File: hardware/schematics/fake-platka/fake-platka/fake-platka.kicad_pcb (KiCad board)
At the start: 2 copper layers, 13.5 x 1.1 mm, 27 parts, among them J1 XT60PW-F, J2 XT60PW-F, J3 B2B-EH-A, J4 B2B-EH-A, J5 B2B-EH-A, J6 B2B-EH-A, J7 B2B-EH-A, J8 XT60PW-F, J9 XT60PW-F, U1 XL4005, U2 TB67H450AFNG_EL, U3 TB67H450AFNG_EL, U4 SC0915-pico-w-board, U5 XL4005

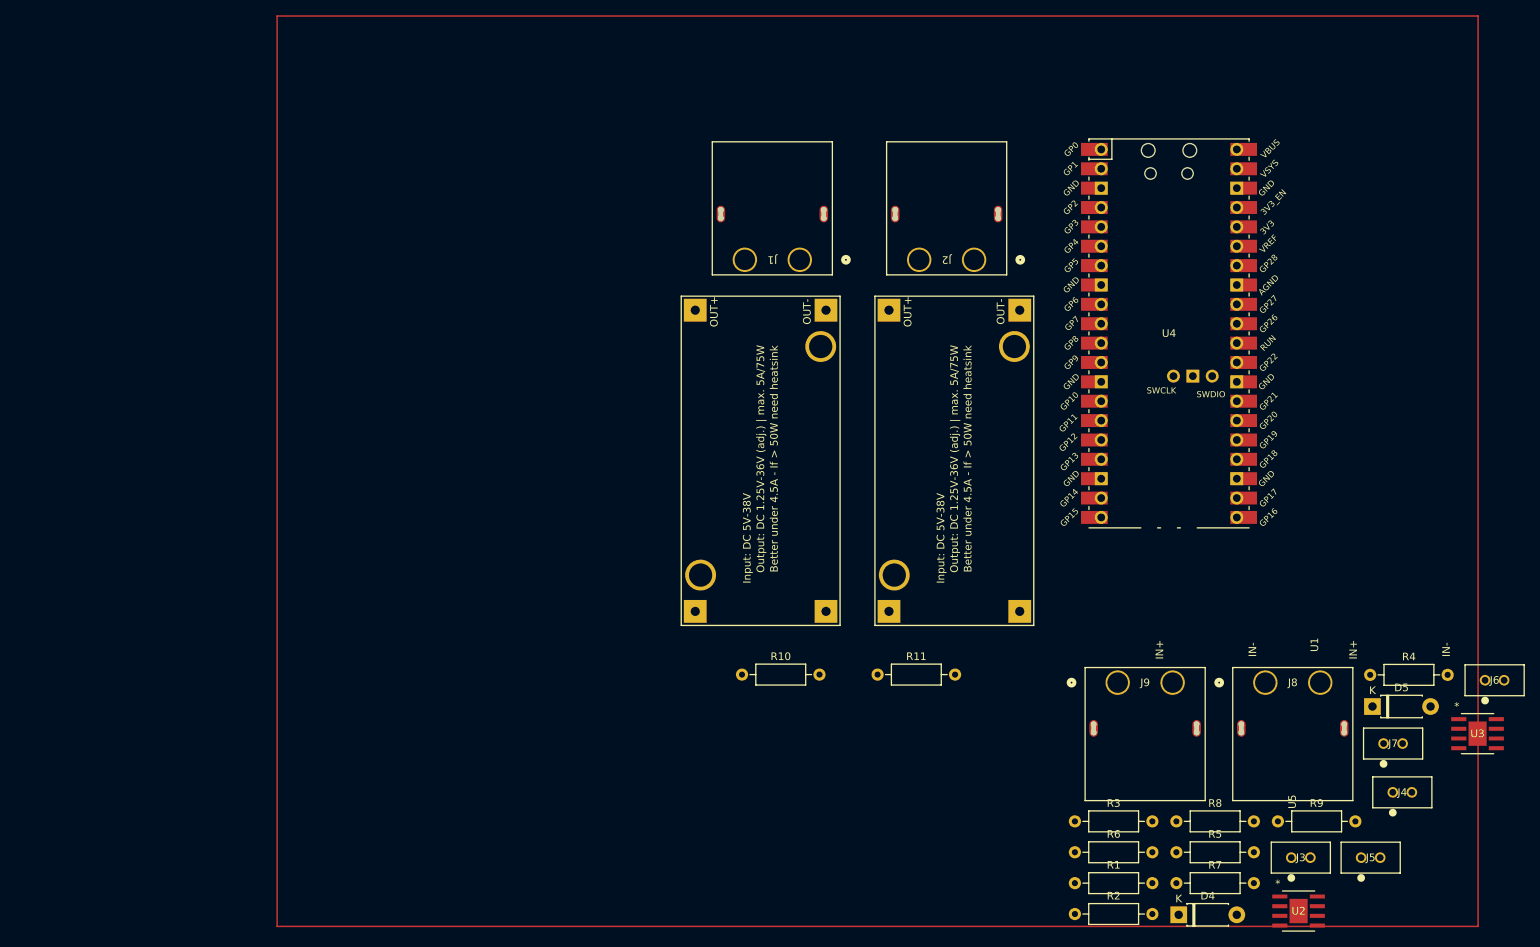
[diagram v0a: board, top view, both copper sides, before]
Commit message: added all components to the schematic and pcb
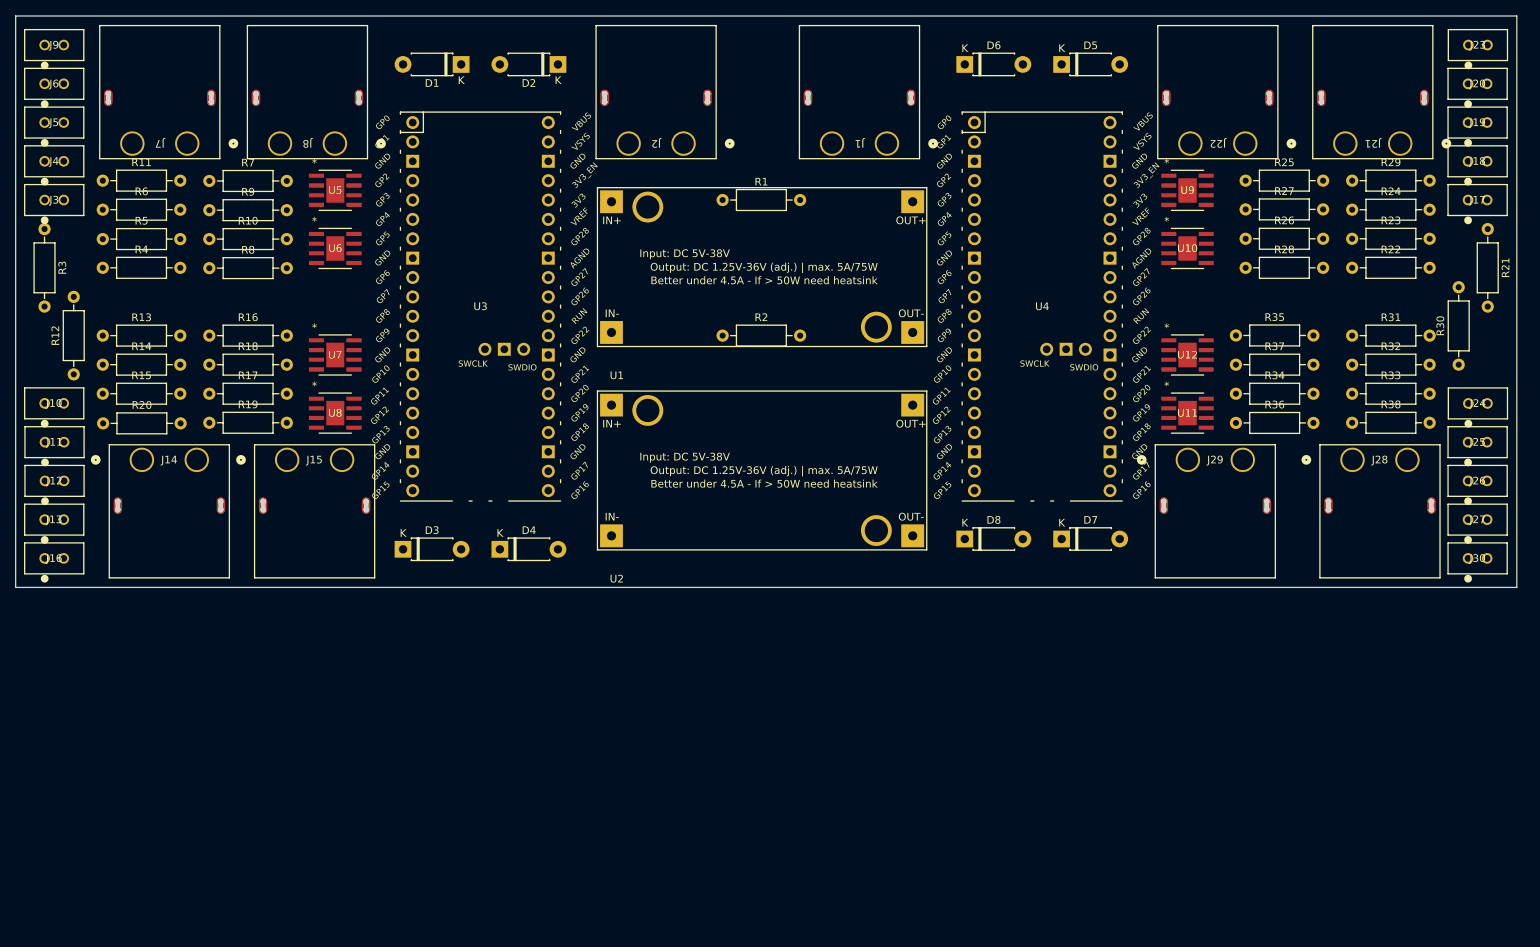
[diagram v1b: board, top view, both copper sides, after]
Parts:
- added D1: 1N4001, Diode_THT:D_DO-41_SOD81_P7.62mm_Horizontal, F.Cu at (90.2, 39.4)
- added D2: 1N4001, Diode_THT:D_DO-41_SOD81_P7.62mm_Horizontal, F.Cu at (102.9, 39.4)
- added D3: 1N4001, Diode_THT:D_DO-41_SOD81_P7.62mm_Horizontal, F.Cu at (82.5, 103.0)
- added D6: 1N4001, Diode_THT:D_DO-41_SOD81_P7.62mm_Horizontal, F.Cu at (156.2, 39.4)
- added D7: 1N4001, Diode_THT:D_DO-41_SOD81_P7.62mm_Horizontal, F.Cu at (168.9, 101.6)
- added D8: 1N4001, Diode_THT:D_DO-41_SOD81_P7.62mm_Horizontal, F.Cu at (156.2, 101.6)
- added J10: B2B-EH-A, quadruped-lib-footprints:CONN_B2B-EH-A LFSN_JST, F.Cu at (35.6, 83.8)
- added J11: B2B-EH-A, quadruped-lib-footprints:CONN_B2B-EH-A LFSN_JST, F.Cu at (35.6, 88.9)
- added J12: B2B-EH-A, quadruped-lib-footprints:CONN_B2B-EH-A LFSN_JST, F.Cu at (35.6, 94.0)
- added J13: B2B-EH-A, quadruped-lib-footprints:CONN_B2B-EH-A LFSN_JST, F.Cu at (35.6, 99.1)
- added J14: XT60PW-F, quadruped-lib-footprints:CONN_XT60PW-F_AMA, F.Cu at (48.3, 91.2)
- added J15: XT60PW-F, quadruped-lib-footprints:CONN_XT60PW-F_AMA, F.Cu at (67.4, 91.2)
- added J16: B2B-EH-A, quadruped-lib-footprints:CONN_B2B-EH-A LFSN_JST, F.Cu at (35.6, 104.1)
- added J17: B2B-EH-A, quadruped-lib-footprints:CONN_B2B-EH-A LFSN_JST, F.Cu at (222.2, 57.1)
- added J18: B2B-EH-A, quadruped-lib-footprints:CONN_B2B-EH-A LFSN_JST, F.Cu at (222.2, 52.1)
- added J19: B2B-EH-A, quadruped-lib-footprints:CONN_B2B-EH-A LFSN_JST, F.Cu at (222.2, 47.0)
- added J20: B2B-EH-A, quadruped-lib-footprints:CONN_B2B-EH-A LFSN_JST, F.Cu at (222.2, 41.9)
- added J21: XT60PW-F, quadruped-lib-footprints:CONN_XT60PW-F_AMA, F.Cu at (213.3, 49.7)
- added J22: XT60PW-F, quadruped-lib-footprints:CONN_XT60PW-F_AMA, F.Cu at (193.0, 49.7)
- added J23: B2B-EH-A, quadruped-lib-footprints:CONN_B2B-EH-A LFSN_JST, F.Cu at (222.2, 36.8)
- added J24: B2B-EH-A, quadruped-lib-footprints:CONN_B2B-EH-A LFSN_JST, F.Cu at (222.2, 83.8)
- added J25: B2B-EH-A, quadruped-lib-footprints:CONN_B2B-EH-A LFSN_JST, F.Cu at (222.2, 88.9)
- added J26: B2B-EH-A, quadruped-lib-footprints:CONN_B2B-EH-A LFSN_JST, F.Cu at (222.2, 94.0)
- added J27: B2B-EH-A, quadruped-lib-footprints:CONN_B2B-EH-A LFSN_JST, F.Cu at (222.2, 99.1)
- added J28: XT60PW-F, quadruped-lib-footprints:CONN_XT60PW-F_AMA, F.Cu at (207.1, 91.2)
- added J29: XT60PW-F, quadruped-lib-footprints:CONN_XT60PW-F_AMA, F.Cu at (185.5, 91.2)
- added J30: B2B-EH-A, quadruped-lib-footprints:CONN_B2B-EH-A LFSN_JST, F.Cu at (222.2, 104.1)
- added R12: 5K, Resistor_THT:R_Axial_DIN0207_L6.3mm_D2.5mm_P10.16mm_Horizontal, F.Cu at (39.4, 80.0)
- added R13: 5K, Resistor_THT:R_Axial_DIN0207_L6.3mm_D2.5mm_P10.16mm_Horizontal, F.Cu at (43.2, 74.9)
- added R14: 150R, Resistor_THT:R_Axial_DIN0207_L6.3mm_D2.5mm_P10.16mm_Horizontal, F.Cu at (43.2, 78.7)
- added R15: 5K, Resistor_THT:R_Axial_DIN0207_L6.3mm_D2.5mm_P10.16mm_Horizontal, F.Cu at (43.2, 82.5)
- added R16: R1, Resistor_THT:R_Axial_DIN0207_L6.3mm_D2.5mm_P10.16mm_Horizontal, F.Cu at (57.1, 74.9)
- added R17: R1, Resistor_THT:R_Axial_DIN0207_L6.3mm_D2.5mm_P10.16mm_Horizontal, F.Cu at (57.1, 82.5)
- added R18: R1, Resistor_THT:R_Axial_DIN0207_L6.3mm_D2.5mm_P10.16mm_Horizontal, F.Cu at (57.1, 78.7)
- added R19: R1, Resistor_THT:R_Axial_DIN0207_L6.3mm_D2.5mm_P10.16mm_Horizontal, F.Cu at (57.1, 86.4)
- added R20: 5K, Resistor_THT:R_Axial_DIN0207_L6.3mm_D2.5mm_P10.16mm_Horizontal, F.Cu at (43.2, 86.4)
- added R21: 5K, Resistor_THT:R_Axial_DIN0207_L6.3mm_D2.5mm_P10.16mm_Horizontal, F.Cu at (224.8, 61.0)
- added R22: 5K, Resistor_THT:R_Axial_DIN0207_L6.3mm_D2.5mm_P10.16mm_Horizontal, F.Cu at (207.0, 66.0)
- added R23: 150R, Resistor_THT:R_Axial_DIN0207_L6.3mm_D2.5mm_P10.16mm_Horizontal, F.Cu at (207.0, 62.2)
- added R24: 5K, Resistor_THT:R_Axial_DIN0207_L6.3mm_D2.5mm_P10.16mm_Horizontal, F.Cu at (207.0, 58.4)
- added R25: R1, Resistor_THT:R_Axial_DIN0207_L6.3mm_D2.5mm_P10.16mm_Horizontal, F.Cu at (193.0, 54.6)
- added R26: R1, Resistor_THT:R_Axial_DIN0207_L6.3mm_D2.5mm_P10.16mm_Horizontal, F.Cu at (193.0, 62.2)
- added R27: R1, Resistor_THT:R_Axial_DIN0207_L6.3mm_D2.5mm_P10.16mm_Horizontal, F.Cu at (193.0, 58.4)
- added R28: R1, Resistor_THT:R_Axial_DIN0207_L6.3mm_D2.5mm_P10.16mm_Horizontal, F.Cu at (193.0, 66.0)
- added R29: 5K, Resistor_THT:R_Axial_DIN0207_L6.3mm_D2.5mm_P10.16mm_Horizontal, F.Cu at (207.0, 54.6)
- added R30: 5K, Resistor_THT:R_Axial_DIN0207_L6.3mm_D2.5mm_P10.16mm_Horizontal, F.Cu at (221.0, 78.7)
- added R31: 5K, Resistor_THT:R_Axial_DIN0207_L6.3mm_D2.5mm_P10.16mm_Horizontal, F.Cu at (207.0, 74.9)
- added R32: 150R, Resistor_THT:R_Axial_DIN0207_L6.3mm_D2.5mm_P10.16mm_Horizontal, F.Cu at (207.0, 78.7)
- added R33: 5K, Resistor_THT:R_Axial_DIN0207_L6.3mm_D2.5mm_P10.16mm_Horizontal, F.Cu at (207.0, 82.5)
- added R34: R1, Resistor_THT:R_Axial_DIN0207_L6.3mm_D2.5mm_P10.16mm_Horizontal, F.Cu at (191.8, 82.5)
- added R35: R1, Resistor_THT:R_Axial_DIN0207_L6.3mm_D2.5mm_P10.16mm_Horizontal, F.Cu at (191.8, 74.9)
- added R36: R1, Resistor_THT:R_Axial_DIN0207_L6.3mm_D2.5mm_P10.16mm_Horizontal, F.Cu at (191.8, 86.4)
- added R37: R1, Resistor_THT:R_Axial_DIN0207_L6.3mm_D2.5mm_P10.16mm_Horizontal, F.Cu at (191.8, 78.7)
- added R38: 5K, Resistor_THT:R_Axial_DIN0207_L6.3mm_D2.5mm_P10.16mm_Horizontal, F.Cu at (207.0, 86.4)
- added U10: TB67H450AFNG_EL, quadruped-lib-footprints:P-HSOP8-0405-1.27-002_TOS, F.Cu at (185.4, 63.5)
- added U11: TB67H450AFNG_EL, quadruped-lib-footprints:P-HSOP8-0405-1.27-002_TOS, F.Cu at (185.4, 85.1)
- added U12: TB67H450AFNG_EL, quadruped-lib-footprints:P-HSOP8-0405-1.27-002_TOS, F.Cu at (185.4, 77.5)
- added U6: TB67H450AFNG_EL, quadruped-lib-footprints:P-HSOP8-0405-1.27-002_TOS, F.Cu at (73.7, 63.5)
- added U7: TB67H450AFNG_EL, quadruped-lib-footprints:P-HSOP8-0405-1.27-002_TOS, F.Cu at (73.7, 77.5)
- added U8: TB67H450AFNG_EL, quadruped-lib-footprints:P-HSOP8-0405-1.27-002_TOS, F.Cu at (73.7, 85.1)
- added U9: TB67H450AFNG_EL, quadruped-lib-footprints:P-HSOP8-0405-1.27-002_TOS, F.Cu at (185.4, 55.9)
- D4, D5: value DIODE -> 1N4001
- J7: value B2B-EH-A -> XT60PW-F; footprint quadruped-lib-footprints:CONN_B2B-EH-A LFSN_JST -> quadruped-lib-footprints:CONN_XT60PW-F_AMA
- J9: value XT60PW-F -> B2B-EH-A; footprint quadruped-lib-footprints:CONN_XT60PW-F_AMA -> quadruped-lib-footprints:CONN_B2B-EH-A LFSN_JST
- R1, R7: value 5K -> R1
- R11, R6: value R1 -> 5K
- R2: value 150R -> R1
- R5: value R1 -> 150R
- U2: value TB67H450AFNG_EL -> XL4005; footprint quadruped-lib-footprints:P-HSOP8-0405-1.27-002_TOS -> quadruped-lib-footprints:XL4005_DC-DC
- U3: value TB67H450AFNG_EL -> SC0915-pico-w-board; footprint quadruped-lib-footprints:P-HSOP8-0405-1.27-002_TOS -> quadruped-lib-footprints:RPi_PicoW_SMD_TH
- U5: value XL4005 -> TB67H450AFNG_EL; footprint quadruped-lib-footprints:XL4005_DC-DC -> quadruped-lib-footprints:P-HSOP8-0405-1.27-002_TOS
- moved J6 204.4 mm to (35.6, 41.9)
- moved J5 197.7 mm to (35.6, 47.0)
- moved J4 195.2 mm to (35.6, 52.1)
- moved J3 184.8 mm to (35.6, 57.1)
- moved J7 175.5 mm to (54.3, 49.7), turned to 180 degrees
- moved R4 174.6 mm to (43.2, 66.0)
- moved J9 163.7 mm to (35.6, 36.8)
- moved R5 162.1 mm to (43.2, 62.3)
- moved R9 161.4 mm to (57.1, 58.5)
- moved R7 156.7 mm to (57.1, 54.6)
- moved R3 155.8 mm to (35.5, 61.0), turned to -90 degrees
- moved R6 152.8 mm to (43.2, 58.4)
- moved R8 146.1 mm to (57.1, 66.1)
- moved U3 142.2 mm to (92.7, 71.1)
- moved J8 141.0 mm to (73.6, 49.7), turned to 180 degrees
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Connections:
- D4 pad 1: /Leg Back Right/12V -> /Leg Back Left/12V
- D5 pad 1: /Leg Back Right/12V -> /Leg Back Left/12V
- J3 pad 1: /Leg Back Right/3V3 -> /Left Controller /3V3
- J3 pad 2: /Leg Back Right/BR_F_EB -> /Left Controller /FL_F_EB
- J4 pad 1: /Leg Back Right/3V3 -> /Left Controller /3V3
- J4 pad 2: /Leg Back Right/BR_F_EA -> /Left Controller /FL_F_EA
- J5 pad 2: /Leg Back Right/GND3V3 -> /Left Controller /GND3V3
- J6 pad 1: /Leg Back Right/3V3 -> /Left Controller /3V3
- J6 pad 2: /Leg Back Right/BR_K_EB -> /Left Controller /FL_K_EB
- J7 pad 1: /Leg Back Right/3V3 -> Net-(J7-Pad1)
- J7 pad 2: /Leg Back Right/BR_K_EA -> Net-(J7-Pad2)
- J9 pad 1: Net-(J9-Pad1) -> /Left Controller /3V3
- J9 pad 2: Net-(J9-Pad2) -> /Left Controller /FL_K_EA
- R1 pad 1: /Leg Back Right/BR_F_EB -> Net-(J1-Pad2)
- R1 pad 2: /Leg Back Right/GND3V3 -> /Leg Back Left/12V
- R10 pad 1: Net-(J1-Pad2) -> /Leg Back Left/12V
- R10 pad 2: /Leg Back Right/12V -> Net-(R10-Pad2)
- R11 pad 1: Net-(J1-Pad1) -> /Left Controller /FL_K_EA
- R11 pad 2: /Leg Back Right/GND12V -> /Left Controller /GND3V3
- R2 pad 1: Net-(J5-Pad1) -> Net-(J1-Pad1)
- R2 pad 2: /Leg Back Right/3V3 -> /Leg Back Right/GND12V
- R3 pad 1: /Leg Back Right/BR_F_EA -> /Left Controller /FL_F_EB
- R3 pad 2: /Leg Back Right/GND3V3 -> /Left Controller /GND3V3
- R4 pad 1: /Leg Back Right/BR_K_EB -> /Left Controller /FL_F_EA
- R4 pad 2: /Leg Back Right/GND3V3 -> /Left Controller /GND3V3
- R5 pad 1: Net-(R5-Pad1) -> Net-(J5-Pad1)
- R5 pad 2: /Leg Back Right/GND12V -> /Left Controller /3V3
- R6 pad 1: /Leg Back Right/GND12V -> /Left Controller /FL_K_EB
- R6 pad 2: Net-(R6-Pad2) -> /Left Controller /GND3V3
- R7 pad 1: /Leg Back Right/BR_K_EA -> Net-(R7-Pad1)
- R7 pad 2: /Leg Back Right/GND3V3 -> /Leg Back Left/12V
- R8 pad 1: Net-(R5-Pad1) -> /Leg Back Left/12V
- R8 pad 2: /Leg Back Right/GND12V -> Net-(R10-Pad2)
- R9 pad 1: /Leg Back Right/GND12V -> Net-(R7-Pad1)
- R9 pad 2: Net-(R6-Pad2) -> /Leg Back Left/12V
- U1 pad 3: /Leg Back Right/12V -> /Leg Back Left/12V
- U2 pad 1: /Leg Back Right/GND12V -> /Leg Back Left/12V
- U2 pad 2: /Leg Back Right/BR_F_IN2 -> /Leg Back Right/GND12V
- U2 pad 3: /Leg Back Right/BR_F_IN1 -> /Left Controller /3V3
- U2 pad 4: /Leg Back Right/BR_F_VREF -> /Left Controller /GND3V3
- U3 pad 1: /Leg Back Right/GND12V -> /Left Controller /FL_F_IN1
- U3 pad 2: /Leg Back Right/BR_K_IN2 -> /Left Controller /FL_F_IN2
- U3 pad 3: /Leg Back Right/BR_K_IN1 -> unconnected-(U3-Pad3)
- U3 pad 4: /Leg Back Right/BR_F_VREF -> /Left Controller /FL_K_IN1
- U3 pad 5: Net-(D5-Pad2) -> /Left Controller /FL_K_IN2
- U3 pad 6: Net-(J9-Pad2) -> /Left Controller /BL_F_IN1
- U3 pad 7: Net-(R6-Pad2) -> /Left Controller /BL_F_IN2
- U3 pad 8: Net-(J9-Pad1) -> unconnected-(U3-Pad8)
- U4 pad 1: /Right Controller/FR_F_IN1 -> /Leg Front Right/FR_F_IN1
- U4 pad 11: /Right Controller/FR_F_EA -> /Leg Front Right/FR_F_EA
- U4 pad 12: /Right Controller/FR_F_EB -> /Leg Front Right/FR_F_EB
- U4 pad 14: /Right Controller/FR_K_EA -> /Leg Front Right/FR_K_EA
- U4 pad 15: /Right Controller/FR_K_EB -> /Leg Front Right/FR_K_EB
- U4 pad 2: /Right Controller/FR_F_IN2 -> /Leg Front Right/FR_F_IN2
- U4 pad 38: /Leg Back Right/GND3V3 -> /Left Controller /GND3V3
- U4 pad 39: /Leg Back Right/3V3 -> /Left Controller /3V3
- U4 pad 4: /Right Controller/FR_K_IN1 -> /Leg Front Right/FR_K_IN1
- U4 pad 5: /Right Controller/FR_K_IN2 -> /Leg Front Right/FR_K_IN2
- U5 pad 1: /Leg Back Right/12V -> /Leg Back Left/12V
- U5 pad 2: /Leg Back Right/GND12V -> /Left Controller /FL_F_IN2
- U5 pad 3: /Leg Back Right/3V3 -> /Left Controller /FL_F_IN1
- U5 pad 4: /Leg Back Right/GND3V3 -> /Left Controller /3V3_VREF
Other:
- board size 13.5 x 1.1 mm -> 196.8 x 74.9 mm
